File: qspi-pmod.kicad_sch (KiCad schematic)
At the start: 10 parts, among them J1 PMOD, U1 W25Q128JVS, U2 878-APS6404L-3SQR-SN, U3 878-APS6404L-3SQR-SN

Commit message: Fixup
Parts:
- J1: MPN (none) -> 826634-6
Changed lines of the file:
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@@
+      (effects (font (size 1.27 1.27)) hide)
+    )
+    (property "MPN" "826634-6" (at 72.39 92.71 0)
       (effects (font (size 1.27 1.27)) hide)
     )

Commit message: Add optional CLK cap and CS disconnects
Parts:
- added C7: 20pF, Capacitor_SMD:C_0402_1005Metric, symbol Device:C
- added J2: CONFIG, Connector_PinHeader_2.54mm:PinHeader_2x04_P2.54mm_Vertical, symbol Connector_Generic:Conn_02x04_Odd_Even
- added R1, R2, R3: 1k, Resistor_SMD:R_0402_1005Metric, symbol Device:R
- J1: footprint Connector_PinHeader_2.54mm:PinHeader_2x06_P2.54mm_Horizontal -> tt:PinHeader_2x06_P2.54mm_PMODPeriph2B; symbol Connector_Generic:Conn_02x06_Top_Bottom -> tt:PMOD_PERIPH_2x6; LCSC Part (none) -> C492434
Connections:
- net +3.3V: now also R1.2, R2.2, R3.2
- net GND: now also C7.1
- net PMOD1: now also J2.2 (Pin_2), R3.1; no longer J1.1 (Pin_1)
- net PMOD4: now also J2.7 (Pin_7)
- net PMOD7: now also J2.4 (Pin_4), R2.1; no longer J1.9 (Pin_9)
- net PMOD8: now also J2.6 (Pin_6), R1.1; no longer J1.10 (Pin_10)
- new net: C7.2, J2.8 (Pin_8)
- new net PMOD1_IN: J1.1 (IO1), J2.1 (Pin_1)
- new net PMOD7_IN: J1.9 (IO7), J2.3 (Pin_3)
- new net PMOD8_IN: J1.10 (IO8), J2.5 (Pin_5)
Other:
- note added: "CS cut / clock delay"
- note added: "CS pull up"
- title: QSPI-Pmod -> ${TITLE}

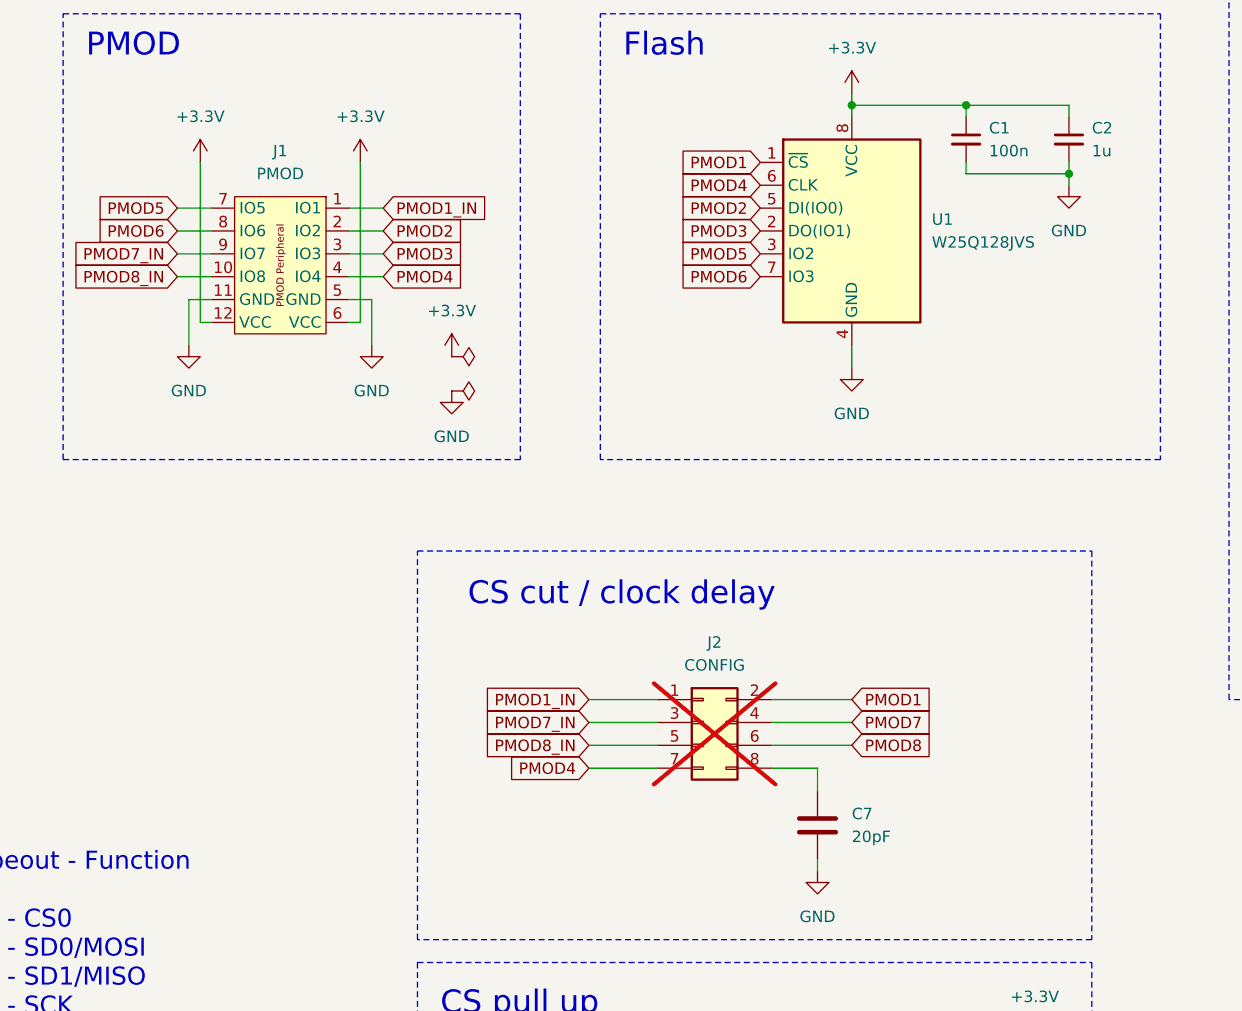
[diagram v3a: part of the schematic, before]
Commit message: Change cap to 22pF
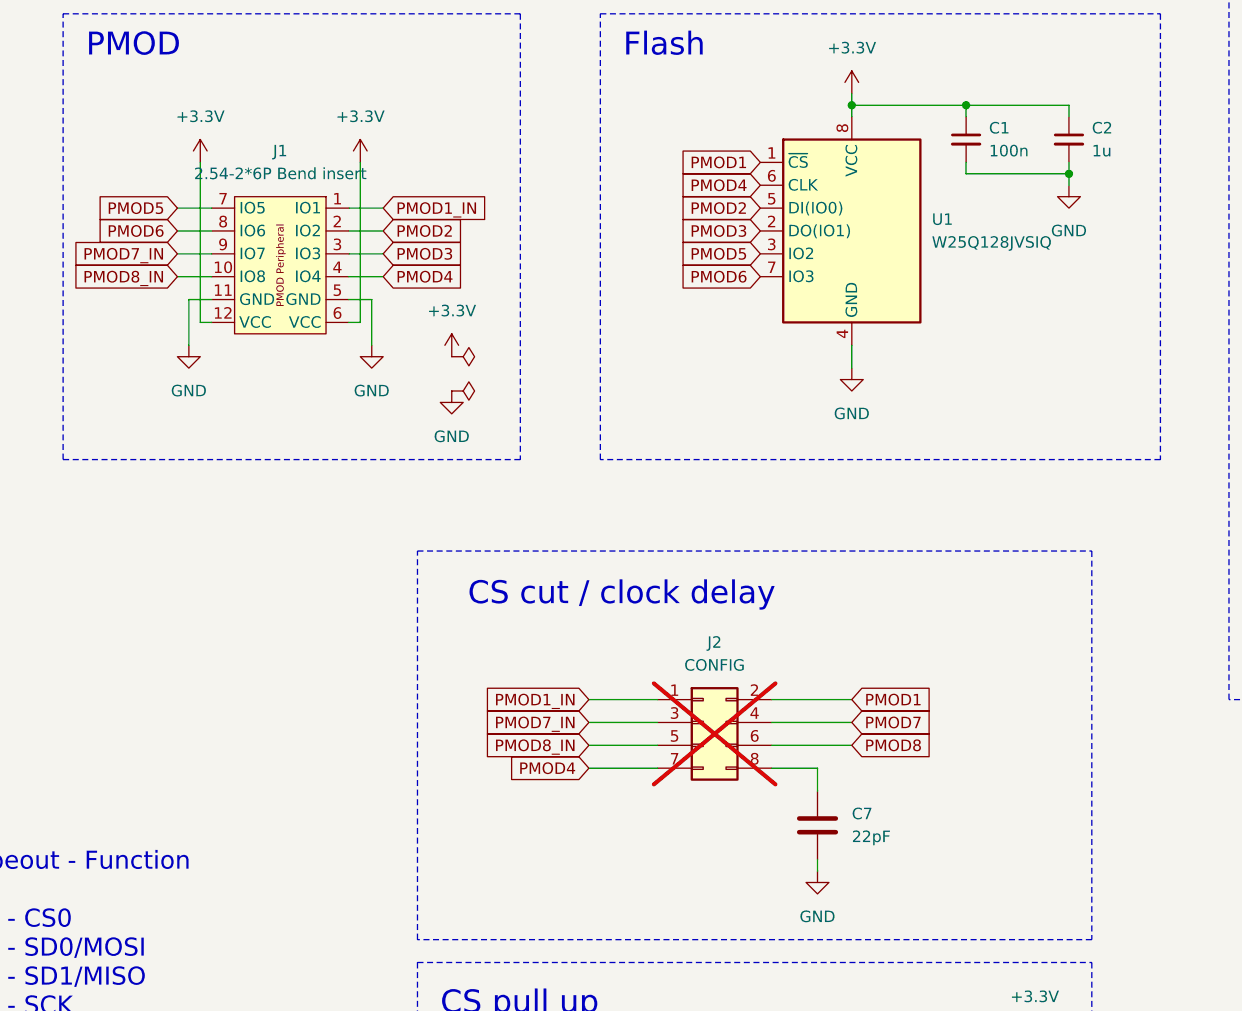
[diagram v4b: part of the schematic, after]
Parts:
- C7: value 20pF -> 22pF
- J1: value PMOD -> 2.54-2*6P Bend insert
- U1: value W25Q128JVS -> W25Q128JVSIQ
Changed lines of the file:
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@@
 			)
 		)
-		(property "Value" "PMOD"
+		(property "Value" "2.54-2*6P Bend insert"
 			(at 71.12 83.82 0)
 			(effects
@@
 			)
 		)
-		(property "Value" "20pF"
+		(property "Value" "22pF"
 			(at 134.62 157.4799 0)
 			(effects
@@
 		(fields_autoplaced yes)
 		(property "Reference" "U1"
-			(at 143.51 88.9 0)
+			(at 143.51 88.8999 0)
 			(effects
 				(font
@@
 			)
 		)
-		(property "Value" "W25Q128JVS"
-			(at 143.51 91.44 0)
-			(effects
-				(font
+		(property "Value" "W25Q128JVSIQ"
+			(at 143.51 91.4399 0)
+			(effects
+				(font

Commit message: BOM updates
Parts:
- C7: MPN (none) -> 0402CG220J500NT
- J1: LCSC Part C492434 -> C60565; MPN 826634-6 -> 2.54-2*6P
- R1, R2, R3: MPN (none) -> 0402WGF1001TCE
- U1: value W25Q128JVSIQ -> W25Q128JVSIM
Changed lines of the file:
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@@
+			)
+		)
+		(property "MPN" "0402WGF1001TCE"
+			(at 130.81 190.5 90)
+			(effects
+				(font
+					(size 1.27 1.27)
+				)
+				(hide yes)
 			)
 		)
@@
 			)
 		)
-		(property "MPN" "826634-6"
+		(property "MPN" "2.54-2*6P"
 			(at 71.12 97.79 0)
 			(effects
@@
 			)
 		)
-		(property "LCSC Part" "C492434"
+		(property "LCSC Part" "C60565"
 			(at 71.1662 108.6699 0)
 			(effects
@@
 			)
 		)
+		(property "MPN" "0402CG220J500NT"
+			(at 130.81 156.21 0)
+			(effects
+				(font
+					(size 1.27 1.27)
+				)
+				(hide yes)
+			)
+		)
 		(pin "2"
 		)
@@
 			)
 		)
-		(property "Value" "W25Q128JVSIQ"
+		(property "Value" "W25Q128JVSIM"
 			(at 143.51 91.4399 0)
 			(effects
@@
 			)
 		)
+		(property "MPN" "0402WGF1001TCE"
+			(at 146.05 185.42 90)
+			(effects
+				(font
+					(size 1.27 1.27)
+				)
+				(hide yes)
+			)
+		)
 		(pin "1"
 		)
@@
 			(effects
 				(font
+					(size 1.27 1.27)
+				)
+				(hide yes)
+			)
+		)
+		(property "MPN" "0402WGF1001TCE"
+			(at 138.43 187.96 90)
+			(effects
+				(font

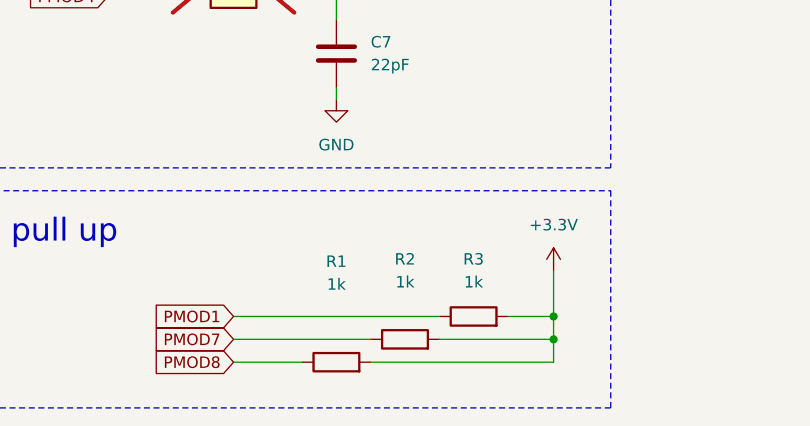
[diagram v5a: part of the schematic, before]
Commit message: Make pull ups 10k
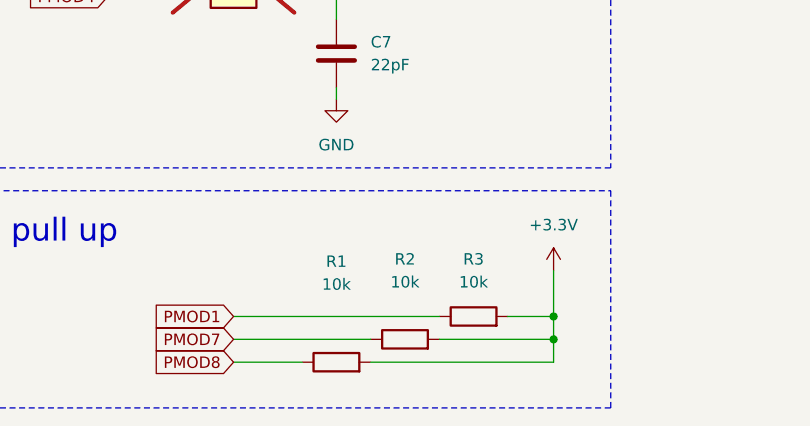
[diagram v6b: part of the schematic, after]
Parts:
- R1, R2, R3: value 1k -> 10k; MPN 0402WGF1001TCE -> 0402WGF1002TCE
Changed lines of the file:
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@@
 (kicad_sch
-	(version 20231120)
+	(version 20250114)
 	(generator "eeschema")
-	(generator_version "8.0")
+	(generator_version "9.0")
 	(paper "A4")
 	(title_block
@@
 		(rev "${REVISION}")
 	)
+	(rectangle
+		(start 106.68 66.04)
+		(end 168.91 115.57)
+		(stroke
+			(width 0)
+			(type dash)
+		)
+		(fill
+			(type none)
+		)
+	)
+	(rectangle
+		(start 176.53 43.18)
+		(end 237.49 142.24)
+		(stroke
+			(width 0)
+			(type dash)
+		)
+		(fill
+			(type none)
+		)
+	)
+	(rectangle
+		(start 46.99 66.04)
+		(end 97.79 115.57)
+		(stroke
+			(width 0)
+			(type dash)
+		)
+		(fill
+			(type none)
+		)
+	)
+	(rectangle
+		(start 86.36 125.73)
+		(end 161.29 168.91)
+		(stroke
+			(width 0)
+			(type dash)
+		)
+		(fill
+			(type none)
+		)
+	)
+	(rectangle
+		(start 86.36 171.45)
+		(end 161.29 195.58)
+		(stroke
+			(width 0)
+			(type dash)
+		)
+		(fill
+			(type none)
+		)
+	)
+	(text "CS cut / clock delay"
+		(exclude_from_sim no)
+		(at 91.948 132.08 0)
+		(effects
+			(font
+				(size 2.54 2.54)
+			)
+			(justify left bottom)
+		)
+	)
+	(text "PMOD"
+		(exclude_from_sim no)
+		(at 49.53 71.12 0)
+		(effects
+			(font
+				(size 2.54 2.54)
+			)
+			(justify left bottom)
+		)
+	)
+	(text "Flash"
+		(exclude_from_sim no)
+		(at 109.22 71.12 0)
+		(effects
+			(font
+				(size 2.54 2.54)
+			)
+			(justify left bottom)
+		)
+	)
+	(text "PSRAM B"
+		(exclude_from_sim no)
+		(at 179.07 95.25 0)
+		(effects
+			(font
+				(size 2.54 2.54)
+			)
+			(justify left bottom)
+		)
+	)
+	(text "CS pull up"
+		(exclude_from_sim no)
+		(at 88.9 177.546 0)
+		(effects
+			(font
+				(size 2.54 2.54)
+			)
+			(justify left bottom)
+		)
+	)
+	(text "${TITLE} ${REVISION}"
+		(exclude_from_sim no)
+		(at 16.51 24.13 0)
+		(effects
+			(font
+				(size 5 5)
+				(bold yes)
+			)
+			(justify left bottom)
+		)
+	)
+	(text "PSRAM A"
+		(exclude_from_sim no)
+		(at 179.07 48.26 0)
+		(effects
+			(font
+				(size 2.54 2.54)
+			)
+			(justify left bottom)
+		)
+	)
+	(text "Pmod - TinyTapeout - Function\n\nPMOD1 - uio[0] - CS0\nPMOD2 - uio[1] - SD0/MOSI\nPMOD3 - uio[2] - SD1/MISO\nPMOD4 - uio[3] - SCK\nPMOD5 - uio[4] - SD2\nPMOD6 - uio[5] - SD3\nPMOD7 - uio[6] - CS1\nPMOD8 - uio[7] - CS2"
+		(exclude_from_sim no)
+		(at 19.05 190.5 0)
+		(effects
+			(font
+				(size 2 2)
+			)
+			(justify left bottom)
+		)
+	)
+	(text "Pinout"
+		(exclude_from_sim no)
+		(at 19.05 154.94 0)
+		(effects
+			(font
+				(size 2.54 2.54)
+				(thickness 0.508)
+				(bold yes)
+			)
+			(justify left bottom)
+		)
+	)
 	(junction
 		(at 147.32 76.2)
@@
 		)
 	)
-	(rectangle
-		(start 106.68 66.04)
-		(end 168.91 115.57)
-		(stroke
-			(width 0)
-			(type dash)
-		)
-		(fill
-			(type none)
-		)
-	)
-	(rectangle
-		(start 176.53 43.18)
-		(end 237.49 142.24)
-		(stroke
-			(width 0)
-			(type dash)
-		)
-		(fill
-			(type none)
-		)
-	)
-	(rectangle
-		(start 46.99 66.04)
-		(end 97.79 115.57)
-		(stroke
-			(width 0)
-			(type dash)
-		)
-		(fill
-			(type none)
-		)
-	)
-	(rectangle
-		(start 86.36 125.73)
-		(end 161.29 168.91)
-		(stroke
-			(width 0)
-			(type dash)
-		)
-		(fill
-			(type none)
-		)
-	)
-	(rectangle
-		(start 86.36 171.45)
-		(end 161.29 195.58)
-		(stroke
-			(width 0)
-			(type dash)
-		)
-		(fill
-			(type none)
-		)
-	)
-	(text "CS cut / clock delay"
-		(exclude_from_sim no)
-		(at 91.948 132.08 0)
-		(effects
-			(font
-				(size 2.54 2.54)
-			)
-			(justify left bottom)
-		)
-	)
-	(text "PMOD"
-		(exclude_from_sim no)
-		(at 49.53 71.12 0)
-		(effects
-			(font
-				(size 2.54 2.54)
-			)
-			(justify left bottom)
-		)
-	)
-	(text "Flash"
-		(exclude_from_sim no)
-		(at 109.22 71.12 0)
-		(effects
-			(font
-				(size 2.54 2.54)
-			)
-			(justify left bottom)
-		)
-	)
-	(text "PSRAM B"
-		(exclude_from_sim no)
-		(at 179.07 95.25 0)
-		(effects
-			(font
-				(size 2.54 2.54)
-			)
-			(justify left bottom)
-		)
-	)
-	(text "CS pull up"
-		(exclude_from_sim no)
-		(at 88.9 177.546 0)
-		(effects
-			(font
-				(size 2.54 2.54)
-			)
-			(justify left bottom)
-		)
-	)
-	(text "${TITLE} ${REVISION}"
-		(exclude_from_sim no)
-		(at 16.51 24.13 0)
-		(effects
-			(font
-				(size 5 5)
-				(bold yes)
-			)
-			(justify left bottom)
-		)
-	)
-	(text "PSRAM A"
-		(exclude_from_sim no)
-		(at 179.07 48.26 0)
-		(effects
-			(font
-				(size 2.54 2.54)
-			)
-			(justify left bottom)
-		)
-	)
-	(text "Pmod - TinyTapeout - Function\n\nPMOD1 - uio[0] - CS0\nPMOD2 - uio[1] - SD0/MOSI\nPMOD3 - uio[2] - SD1/MISO\nPMOD4 - uio[3] - SCK\nPMOD5 - uio[4] - SD2\nPMOD6 - uio[5] - SD3\nPMOD7 - uio[6] - CS1\nPMOD8 - uio[7] - CS2"
-		(exclude_from_sim no)
-		(at 19.05 190.5 0)
-		(effects
-			(font
-				(size 2 2)
-			)
-			(justify left bottom)
-		)
-	)
-	(text "Pinout"
-		(exclude_from_sim no)
-		(at 19.05 154.94 0)
-		(effects
-			(font
-				(size 2.54 2.54)
-				(thickness 0.508)
-				(bold yes)
-			)
-			(justify left bottom)
-		)
-	)
 	(global_label "PMOD2"
 		(shape input)
@@
 		(dnp no)
 		(fields_autoplaced yes)
-		(property "Reference" "#PWR016"
+		(property "Reference" "#PWR010"
 			(at 205.74 104.14 0)
 			(effects
@@
 			)
 		)
-		(property "Value" "1k"
+		(property "Value" "10k"
 			(at 130.81 181.864 90)
 			(effects
@@
 			)
 		)
-		(property "MPN" "0402WGF1001TCE"
+		(property "MPN" "0402WGF1002TCE"
 			(at 130.81 190.5 90)
 			(effects
@@
 		(dnp no)
 		(fields_autoplaced yes)
-		(property "Reference" "#PWR017"
+		(property "Reference" "#PWR08"
 			(at 134.62 111.76 0)
 			(effects
@@
 		(dnp no)
 		(fields_autoplaced yes)
-		(property "Reference" "#PWR017"
+		(property "Reference" "#PWR011"
 			(at 205.74 135.89 0)
 			(effects
@@
 		(dnp no)
 		(fields_autoplaced yes)
-		(property "Reference" "#PWR016"
+		(property "Reference" "#PWR05"
 			(at 90.17 107.95 0)
 			(effects
@@
 		(dnp no)
 		(fields_autoplaced yes)
-		(property "Reference" "#PWR017"
+		(property "Reference" "#PWR06"
 			(at 90.17 114.3 0)
 			(effects
@@
 		(dnp no)
 		(fields_autoplaced yes)
-		(property "Reference" "#PWR03"
+		(property "Reference" "#PWR01"
 			(at 62.23 86.36 0)
 			(effects
@@
 		(dnp no)
 		(fields_autoplaced yes)
-		(property "Reference" "#PWR016"
+		(property "Reference" "#PWR07"
 			(at 134.62 78.74 0)
 			(effects
@@
 		(dnp no)
 		(fields_autoplaced yes)
-		(property "Reference" "#PWR017"
+		(property "Reference" "#PWR09"
 			(at 158.75 91.44 0)
 			(effects
@@
 		(dnp no)
 		(fields_autoplaced yes)
-		(property "Reference" "#PWR017"
+		(property "Reference" "#PWR015"
 			(at 228.6 69.85 0)
 			(effects
@@
 			)
 		)
-		(property "Value" "1k"
+		(property "Value" "10k"
 			(at 146.05 181.61 90)
 			(effects
@@
 			)
 		)
-		(property "MPN" "0402WGF1001TCE"
+		(property "MPN" "0402WGF1002TCE"
 			(at 146.05 185.42 90)
 			(effects
@@
 		(dnp no)
 		(fields_autoplaced yes)
-		(property "Reference" "#PWR016"
+		(property "Reference" "#PWR013"
 			(at 205.74 57.15 0)
 			(effects
@@
 		(dnp no)
 		(fields_autoplaced yes)
-		(property "Reference" "#PWR017"
+		(property "Reference" "#PWR014"
 			(at 205.74 88.9 0)
 			(effects
@@
 			)
 		)
-		(property "Value" "1k"
+		(property "Value" "10k"
 			(at 138.43 181.61 90)
 			(effects
@@
 			)
 		)
-		(property "MPN" "0402WGF1001TCE"
+		(property "MPN" "0402WGF1002TCE"
 			(at 138.43 187.96 90)
 			(effects
@@
 		(dnp no)
 		(fields_autoplaced yes)
-		(property "Reference" "#PWR05"
+		(property "Reference" "#PWR03"
 			(at 81.28 109.22 0)
 			(effects
@@
 		(dnp no)
 		(fields_autoplaced yes)
-		(property "Reference" "#PWR017"
+		(property "Reference" "#PWR012"
 			(at 228.6 116.84 0)
 			(effects
@@
 		)
 	)
+	(embedded_fonts no)
 )
